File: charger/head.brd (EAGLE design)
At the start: 50.8 x 50.8 mm, 5 parts

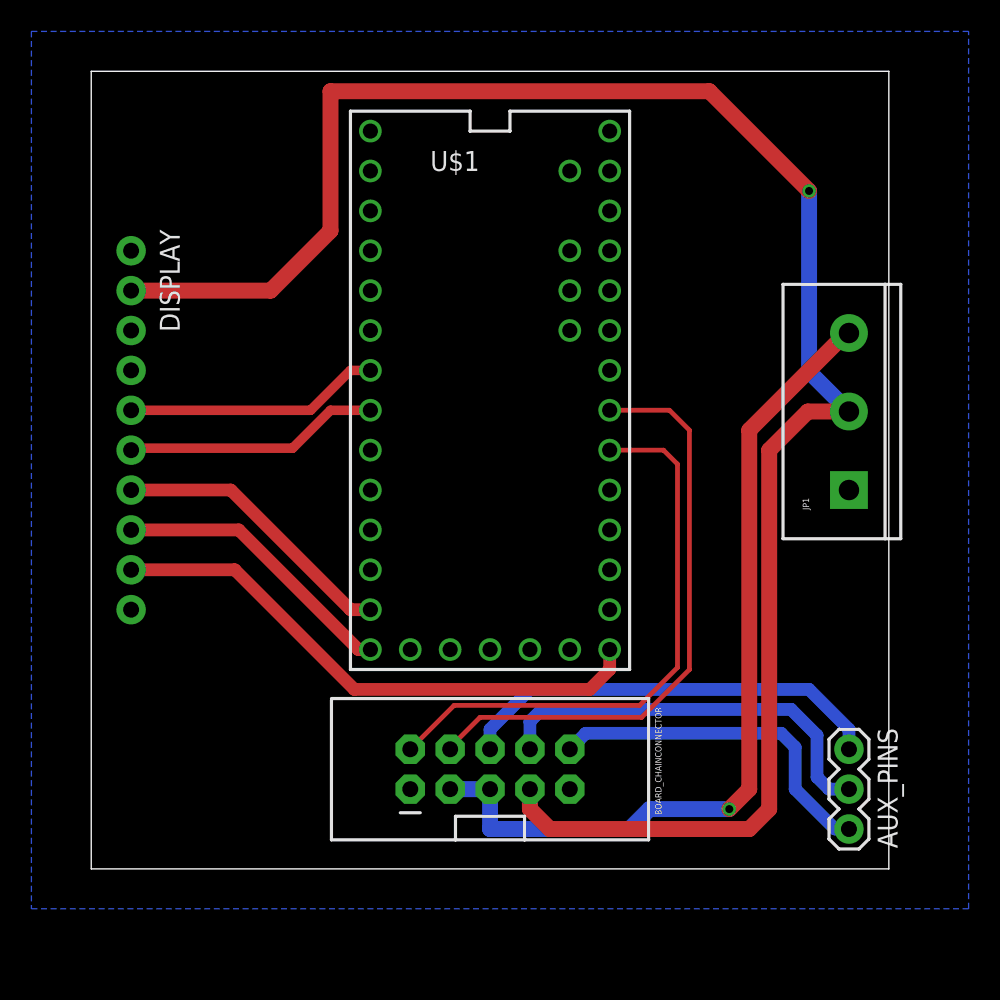
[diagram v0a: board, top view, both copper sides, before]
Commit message: Improve the design and layout of the charger head
- smaller board
- wire up Teensy to power
- add ws2812 status led
- add filtering caps
- add mounting holes
- downgrade to 3x2 header for interboard comms
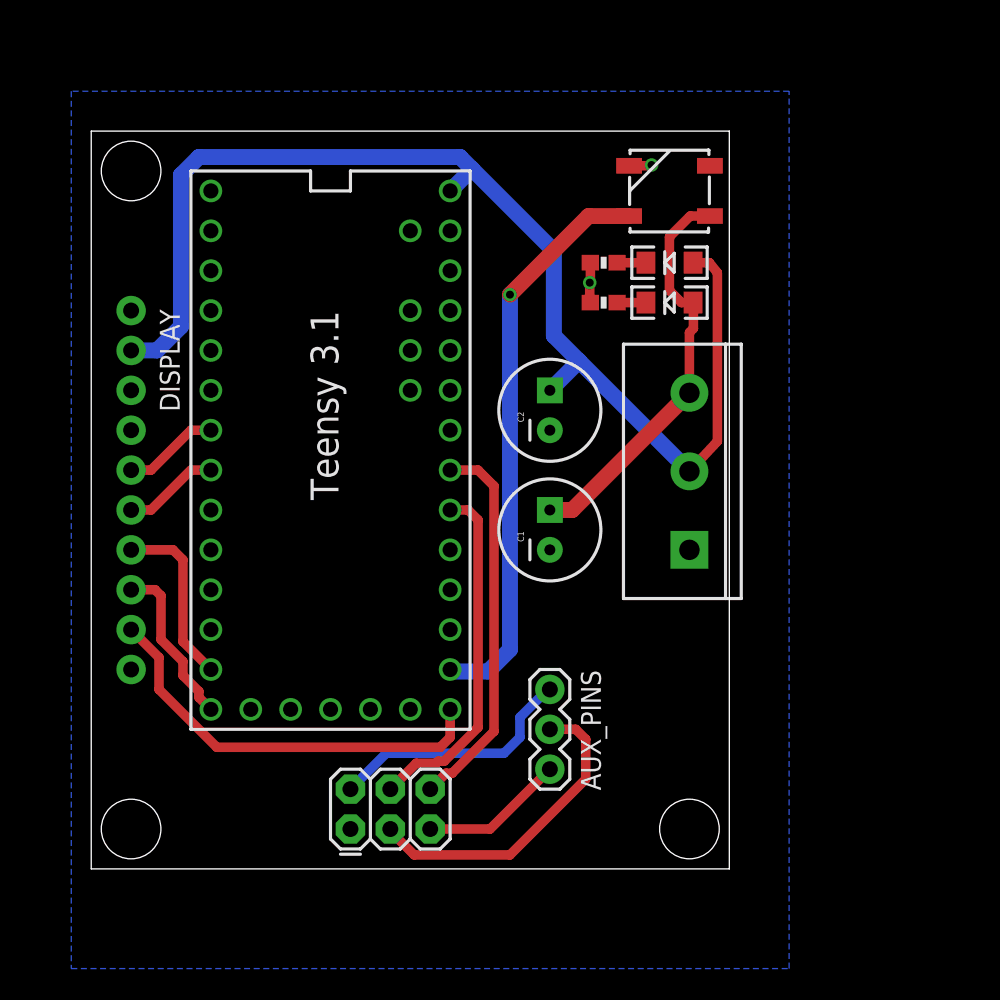
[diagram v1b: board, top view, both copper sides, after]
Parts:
- added C1, C2: (no value), SparkFun-Capacitors:CPOL-RADIAL-100UF-25V
- added D1, D2: RED, SparkFun-LED:LED-1206
- added D3: (no value), SparkFun-LED:WS2812B
- added R1, R2: 200, SparkFun-Resistors:0603-RES
- BOARD_CHAINCONNECTOR: device SparkFun-Connectors:2X5-SHROUDED -> SparkFun-Connectors:2X3
- moved AUX_PINS 19.1 mm to (29.2, 6.35), turned to 90 degrees
- moved U$1 10.9 mm to (15.2, 25.4)
- moved JP1 10.9 mm to (38.1, 20.3)
- moved BOARD_CHAINCONNECTOR 9.67 mm to (16.5, 2.54), turned to 0 degrees
- moved DISPLAY 3.81 mm to (2.54, 35.6)
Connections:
- removed net VIN: U$1.VIN
- new net N$4: D2.C, R1.1
- new net N$5: D1.C, R2.1
- new net STAT_LED: D3.4, U$1.14/A0
- net 12V: now also C1.1, D1.A, D3.1; no longer BOARD_CHAINCONNECTOR.3, BOARD_CHAINCONNECTOR.5
- net 5V: now also C2.1, D2.A, U$1.VIN; no longer BOARD_CHAINCONNECTOR.7
- net CHAINA_SCL: now also BOARD_CHAINCONNECTOR.6; no longer BOARD_CHAINCONNECTOR.4
- net CHAINA_SDA: now also BOARD_CHAINCONNECTOR.4; no longer BOARD_CHAINCONNECTOR.2
- net GND: now also C1.2, C2.2, D3.3, R1.2, R2.2; no longer BOARD_CHAINCONNECTOR.9
- net N$1: now also BOARD_CHAINCONNECTOR.3; no longer BOARD_CHAINCONNECTOR.8
- net N$2: now also AUX_PINS.1, BOARD_CHAINCONNECTOR.5; no longer AUX_PINS.3, BOARD_CHAINCONNECTOR.10
- net N$3: now also AUX_PINS.3, BOARD_CHAINCONNECTOR.2; no longer AUX_PINS.1, BOARD_CHAINCONNECTOR.6
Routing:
- net 5V: track 117.9 -> 77.6 mm, vias 1 -> 0
- net STAT_LED: track 0.00 -> 36.7 mm, vias 0 -> 1
- net 12V: track 54.4 -> 26.2 mm, vias 1 -> 0
- net CHAINA_SDA: track 36.8 -> 22.5 mm
- net CHAINA_SCL: track 38.3 -> 24.4 mm
- net N$2: track 22.3 -> 9.20 mm
- net N$3: track 27.5 -> 16.1 mm
- net SCREEN_CS: track 16.3 -> 6.13 mm
- net SD_CS: track 16.3 -> 6.13 mm
- net SCREEN_SCK: track 35.4 -> 26.7 mm
- net SCREEN_MISO: track 18.4 -> 10.6 mm
- net SCREEN_MOSI: track 18.4 -> 11.3 mm
- net N$1: track 26.1 -> 20.3 mm
- net GND: track 0.00 -> 4.03 mm, vias 0 -> 2
- net N$5: track 0.00 -> 1.84 mm
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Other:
- board size 50.8 x 50.8 mm -> 40.6 x 47 mm
- board text added: "Teensy 3.1"

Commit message: Add a few nice things to the control head
- break out a bunch of teensy pins
- add a resistor to the ws2812 for reliability
- a bit of rerouting
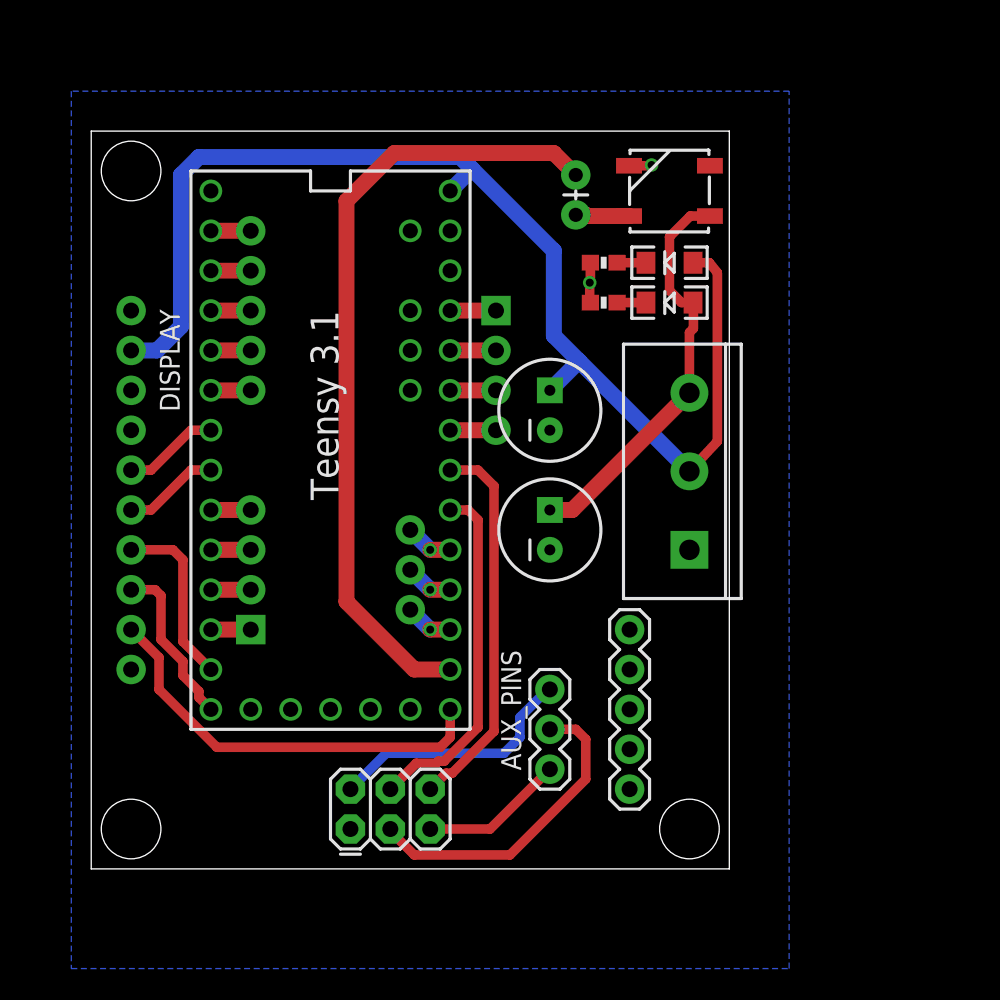
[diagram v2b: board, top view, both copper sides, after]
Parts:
- added JP2, JP3: (no value), SparkFun-Connectors:1X04
- added JP4, JP5: (no value), SparkFun-Connectors:1X05
- added JP6: (no value), SparkFun-Connectors:1X03
- added R3: 330, SparkFun-Resistors:AXIAL-0.1EZ
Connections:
- new net N$10: JP2.2, U$1.22/A8
- new net N$11: JP2.1, U$1.23/A9
- new net N$12: JP3.1, U$1.10
- new net N$13: JP3.2, U$1.9
- new net N$14: JP3.3, U$1.8
- new net N$15: JP3.4, U$1.7
- new net N$16: JP4.1, U$1.4
- new net N$17: JP4.2, U$1.3
- new net N$18: JP4.3, U$1.2
- new net N$19: JP4.4, U$1.1
- new net N$20: JP4.5, U$1.0
- new net N$21: JP6.2, U$1.16/A2
- new net N$22: JP6.1, U$1.17/A3
- new net N$6: D3.4, R3.P$1
- new net N$7: JP6.3, U$1.15/A1
- new net N$8: JP2.4, U$1.20/A6
- new net N$9: JP2.3, U$1.21/A7
- net GND: now also JP5.1, JP5.2, JP5.3, JP5.4, JP5.5
- net STAT_LED: now also R3.P$2; no longer D3.4
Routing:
- net STAT_LED: track 36.7 -> 50.4 mm, vias 1 -> 0
- net N$6: track 0.00 -> 3.42 mm
- net N$7: track 0.00 -> 3.07 mm, vias 0 -> 1
- net N$22: track 0.00 -> 3.07 mm, vias 0 -> 1
- net N$21: track 0.00 -> 3.07 mm, vias 0 -> 1
- net N$9: track 0.00 -> 2.92 mm
- net N$8: track 0.00 -> 2.92 mm
- net N$11: track 0.00 -> 2.92 mm
- net N$10: track 0.00 -> 2.92 mm
- net N$20: track 0.00 -> 2.54 mm
- net N$19: track 0.00 -> 2.54 mm
- net N$18: track 0.00 -> 2.54 mm
- net N$17: track 0.00 -> 2.54 mm
- net N$16: track 0.00 -> 2.54 mm
- net N$15: track 0.00 -> 2.54 mm
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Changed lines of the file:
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@@
 <layer number="23" name="tOrigins" color="15" fill="1" visible="yes" active="yes"/>
 <layer number="24" name="bOrigins" color="15" fill="1" visible="yes" active="yes"/>
-<layer number="25" name="tNames" color="7" fill="1" visible="no" active="yes"/>
-<layer number="26" name="bNames" color="7" fill="1" visible="no" active="yes"/>
-<layer number="27" name="tValues" color="7" fill="1" visible="no" active="yes"/>
-<layer number="28" name="bValues" color="7" fill="1" visible="no" active="yes"/>
+<layer number="25" name="tNames" color="7" fill="1" visible="yes" active="yes"/>
+<layer number="26" name="bNames" color="7" fill="1" visible="yes" active="yes"/>
+<layer number="27" name="tValues" color="7" fill="1" visible="yes" active="yes"/>
+<layer number="28" name="bValues" color="7" fill="1" visible="yes" active="yes"/>
 <layer number="29" name="tStop" color="7" fill="3" visible="no" active="yes"/>
 <layer number="30" name="bStop" color="7" fill="6" visible="no" active="yes"/>
@@
 </element>
 <element name="AUX_PINS" library="SparkFun-Connectors" package="1X03" value="" x="29.21" y="6.35" smashed="yes" rot="R90">
-<attribute name="NAME" x="32.4612" y="5.0038" size="1.27" layer="25" ratio="10" rot="R90"/>
+<attribute name="NAME" x="27.3812" y="6.2738" size="1.27" layer="25" ratio="10" rot="R90"/>
 <attribute name="VALUE" x="32.385" y="5.08" size="1.27" layer="27" rot="R90"/>
 </element>
@@
 <attribute name="VALUE" x="32.576" y="44.78" size="0.6096" layer="27" rot="R180"/>
 </element>
-<element name="C1" library="SparkFun-Capacitors" package="CPOL-RADIAL-100UF-25V" value="" x="29.21" y="21.59" rot="R90">
+<element name="C1" library="SparkFun-Capacitors" package="CPOL-RADIAL-100UF-25V" value="" x="29.21" y="21.59" smashed="yes" rot="R90">
 <attribute name="PROD_ID" value="CAP-08439" x="29.21" y="21.59" size="1.778" layer="27" font="vector" ratio="15" rot="R90" display="off"/>
-</element>
-<element name="C2" library="SparkFun-Capacitors" package="CPOL-RADIAL-100UF-25V" value="" x="29.21" y="29.21" rot="R90">
+<attribute name="VALUE" x="33.528" y="19.685" size="0.8128" layer="27" rot="R90"/>
+</element>
+<element name="C2" library="SparkFun-Capacitors" package="CPOL-RADIAL-100UF-25V" value="" x="29.21" y="29.21" smashed="yes" rot="R90">
 <attribute name="PROD_ID" value="CAP-08439" x="29.21" y="29.21" size="1.778" layer="27" font="vector" ratio="15" rot="R90" display="off"/>
+<attribute name="VALUE" x="33.528" y="27.305" size="0.8128" layer="27" rot="R90"/>
+</element>
+<element name="JP2" library="SparkFun-Connectors" package="1X04" value="" x="25.781" y="35.56" smashed="yes" rot="MR270">
+<attribute name="VALUE" x="28.956" y="36.83" size="1.27" layer="28" rot="MR270"/>
+</element>
+<element name="JP3" library="SparkFun-Connectors" package="1X04" value="" x="10.16" y="15.24" smashed="yes" rot="MR90">
+<attribute name="VALUE" x="6.985" y="13.97" size="1.27" layer="28" rot="MR90"/>
+</element>
+<element name="JP4" library="SparkFun-Connectors" package="1X05" value="" x="10.16" y="30.48" smashed="yes" rot="MR90">
+<attribute name="VALUE" x="6.985" y="29.21" size="1.27" layer="28" rot="MR90"/>
+</element>
+<element name="JP5" library="SparkFun-Connectors" package="1X05" value="" x="34.29" y="5.08" smashed="yes" rot="R90">
+<attribute name="VALUE" x="37.465" y="3.81" size="1.27" layer="27" rot="R90"/>
+</element>
+<element name="R3" library="SparkFun-Resistors" package="AXIAL-0.1EZ" value="330" x="30.861" y="41.656" smashed="yes" rot="R90"/>
+<element name="JP6" library="SparkFun-Connectors" package="1X03" value="" x="20.32" y="21.59" smashed="yes" rot="MR270">
+<attribute name="VALUE" x="23.495" y="22.86" size="1.27" layer="28" rot="MR270"/>
 </element>
 </elements>
@@
 <contactref element="C2" pad="2"/>
 <contactref element="C1" pad="2"/>
+<contactref element="JP5" pad="1"/>
+<contactref element="JP5" pad="2"/>
+<contactref element="JP5" pad="3"/>
+<contactref element="JP5" pad="4"/>
+<contactref element="JP5" pad="5"/>
 </signal>
 <signal name="3.3V">
@@
 </signal>
 <signal name="STAT_LED">
-<contactref element="D3" pad="4"/>
 <contactref element="U$1" pad="14/A0"/>
-<wire x1="34.253" y1="41.58" x2="31.674" y2="41.58" width="1.016" layer="1"/>
-<wire x1="31.674" y1="41.58" x2="26.67" y2="36.576" width="1.016" layer="1"/>
-<via x="26.67" y="36.576" extent="1-16" drill="0.508"/>
-<wire x1="26.67" y1="36.576" x2="26.67" y2="13.97" width="1.016" layer="16"/>
-<wire x1="26.67" y1="13.97" x2="25.273" y2="12.573" width="1.016" layer="16"/>
-<wire x1="25.273" y1="12.573" x2="22.987" y2="12.573" width="1.016" layer="16"/>
-<wire x1="22.987" y1="12.573" x2="22.86" y2="12.7" width="1.016" layer="16"/>
+<wire x1="29.464" y1="45.593" x2="19.304" y2="45.593" width="1.016" layer="1"/>
+<wire x1="19.304" y1="45.593" x2="16.256" y2="42.545" width="1.016" layer="1"/>
+<wire x1="16.256" y1="42.545" x2="16.256" y2="17.018" width="1.016" layer="1"/>
+<wire x1="16.256" y1="17.018" x2="20.574" y2="12.7" width="1.016" layer="1"/>
+<wire x1="20.574" y1="12.7" x2="22.86" y2="12.7" width="1.016" layer="1"/>
+<contactref element="R3" pad="P$2"/>
+<wire x1="29.464" y1="45.593" x2="30.861" y2="44.196" width="1.016" layer="1"/>
 </signal>
 <signal name="N$1">
@@
 <wire x1="18.796" y1="7.366" x2="16.51" y2="5.08" width="0.6096" layer="16"/>
 </signal>
+<signal name="N$8">
+<contactref element="JP2" pad="4"/>
+<contactref element="U$1" pad="20/A6"/>
+<wire x1="22.86" y1="27.94" x2="25.781" y2="27.94" width="1.016" layer="1"/>
+</signal>
+<signal name="N$9">
+<contactref element="JP2" pad="3"/>
+<contactref element="U$1" pad="21/A7"/>
+<wire x1="22.86" y1="30.48" x2="25.781" y2="30.48" width="1.016" layer="1"/>
+</signal>
+<signal name="N$10">
+<contactref element="JP2" pad="2"/>
+<contactref element="U$1" pad="22/A8"/>
+<wire x1="22.86" y1="33.02" x2="25.781" y2="33.02" width="1.016" layer="1"/>
+</signal>
+<signal name="N$11">
+<contactref element="JP2" pad="1"/>
+<contactref element="U$1" pad="23/A9"/>
+<wire x1="25.781" y1="35.56" x2="22.86" y2="35.56" width="1.016" layer="1"/>
+</signal>
+<signal name="N$12">
+<contactref element="JP3" pad="1"/>
+<contactref element="U$1" pad="10"/>
+<wire x1="7.62" y1="15.24" x2="10.16" y2="15.24" width="1.016" layer="1"/>
+</signal>
+<signal name="N$13">
+<contactref element="U$1" pad="9"/>
+<contactref element="JP3" pad="2"/>
+<wire x1="7.62" y1="17.78" x2="10.16" y2="17.78" width="1.016" layer="1"/>
+</signal>
+<signal name="N$14">
+<contactref element="JP3" pad="3"/>
+<contactref element="U$1" pad="8"/>
+<wire x1="7.62" y1="20.32" x2="10.16" y2="20.32" width="1.016" layer="1"/>
+</signal>
+<signal name="N$15">
+<contactref element="U$1" pad="7"/>
+<contactref element="JP3" pad="4"/>
+<wire x1="7.62" y1="22.86" x2="10.16" y2="22.86" width="1.016" layer="1"/>
+</signal>
+<signal name="N$16">
+<contactref element="JP4" pad="1"/>
+<contactref element="U$1" pad="4"/>
+<wire x1="7.62" y1="30.48" x2="10.16" y2="30.48" width="1.016" layer="1"/>
+</signal>
+<signal name="N$17">
+<contactref element="U$1" pad="3"/>
+<contactref element="JP4" pad="2"/>
+<wire x1="7.62" y1="33.02" x2="10.16" y2="33.02" width="1.016" layer="1"/>
+</signal>
+<signal name="N$18">
+<contactref element="JP4" pad="3"/>
+<contactref element="U$1" pad="2"/>
+<wire x1="7.62" y1="35.56" x2="10.16" y2="35.56" width="1.016" layer="1"/>
+</signal>
+<signal name="N$19">
+<contactref element="U$1" pad="1"/>
+<contactref element="JP4" pad="4"/>
+<wire x1="7.62" y1="38.1" x2="10.16" y2="38.1" width="1.016" layer="1"/>
+</signal>
+<signal name="N$20">
+<contactref element="JP4" pad="5"/>
+<contactref element="U$1" pad="0"/>
+<wire x1="7.62" y1="40.64" x2="10.16" y2="40.64" width="1.016" layer="1"/>
+</signal>
+<signal name="N$6">
+<contactref element="D3" pad="4"/>
+<contactref element="R3" pad="P$1"/>
+<wire x1="30.861" y1="41.656" x2="31.5214" y2="41.656" width="1.016" layer="1"/>
+<wire x1="31.5214" y1="41.656" x2="31.5976" y2="41.5798" width="1.016" layer="1"/>
+<wire x1="31.5976" y1="41.5798" x2="34.2528" y2="41.5798" width="1.016" layer="1"/>
+<wire x1="34.2528" y1="41.5798" x2="34.253" y2="41.58" width="1.016" layer="1"/>
+</signal>
+<signal name="N$7">
+<contactref element="JP6" pad="3"/>
+<contactref element="U$1" pad="15/A1"/>
+<wire x1="22.86" y1="15.24" x2="21.59" y2="15.24" width="1.016" layer="1"/>
+<wire x1="21.59" y1="15.24" x2="20.32" y2="16.51" width="1.016" layer="16"/>
+<via x="21.59" y="15.24" extent="1-16" drill="0.508"/>
+</signal>
+<signal name="N$21">
+<contactref element="JP6" pad="2"/>
+<contactref element="U$1" pad="16/A2"/>
+<wire x1="22.86" y1="17.78" x2="21.59" y2="17.78" width="1.016" layer="1"/>
+<wire x1="21.59" y1="17.78" x2="20.32" y2="19.05" width="1.016" layer="16"/>
+<via x="21.59" y="17.78" extent="1-16" drill="0.508"/>
+</signal>
+<signal name="N$22">
+<contactref element="JP6" pad="1"/>
+<contactref element="U$1" pad="17/A3"/>
+<wire x1="22.86" y1="20.32" x2="21.59" y2="20.32" width="1.016" layer="1"/>
+<wire x1="21.59" y1="20.32" x2="20.32" y2="21.59" width="1.016" layer="16"/>
+<via x="21.59" y="20.32" extent="1-16" drill="0.508"/>
+</signal>
 </signals>
